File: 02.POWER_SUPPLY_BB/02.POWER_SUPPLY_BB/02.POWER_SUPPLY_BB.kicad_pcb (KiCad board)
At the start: 2 copper layers, 36.1 x 55.1 mm, 17 parts, among them J1 Conn_01x02_Pin, J2 Conn_01x02_Pin, J3 Conn_01x03_Pin, J4 Conn_01x03_Pin, J5 Screw_Terminal_01x02, J6 Barrel_Jack_Switch, J7 Screw_Terminal_01x02, U1 LM7806_TO220, U2 LM317_TO-220

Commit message: UI
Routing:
- net /3.3v: track 0.00 -> 138.7 mm, vias 0 -> 4
- net GND: track 0.00 -> 120.7 mm
- net /PWR_output: track 0.00 -> 100.6 mm
- net /12V: track 0.00 -> 64.3 mm, vias 0 -> 3
- net /5V: track 0.00 -> 61.3 mm
- net Net-(U2-ADJ): track 0.00 -> 42.4 mm
- net /PWR_input: track 0.00 -> 41.4 mm
- net Net-(D1-A): track 0.00 -> 10.6 mm
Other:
- board text added: "Gobal Krishnan V Practice 0.0.2"

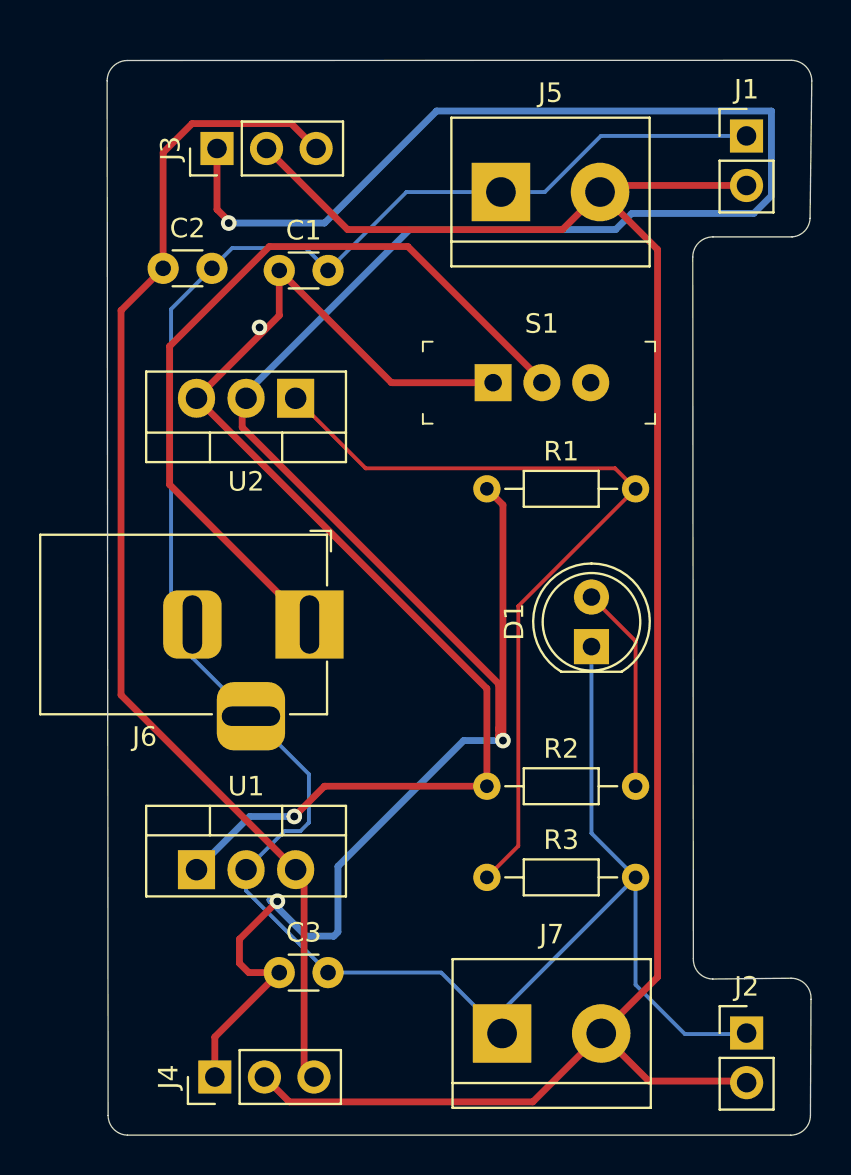
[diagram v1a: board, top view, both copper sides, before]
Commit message: POWER SUPPLY BB - PCB - CHANGE AUTO ROUTING
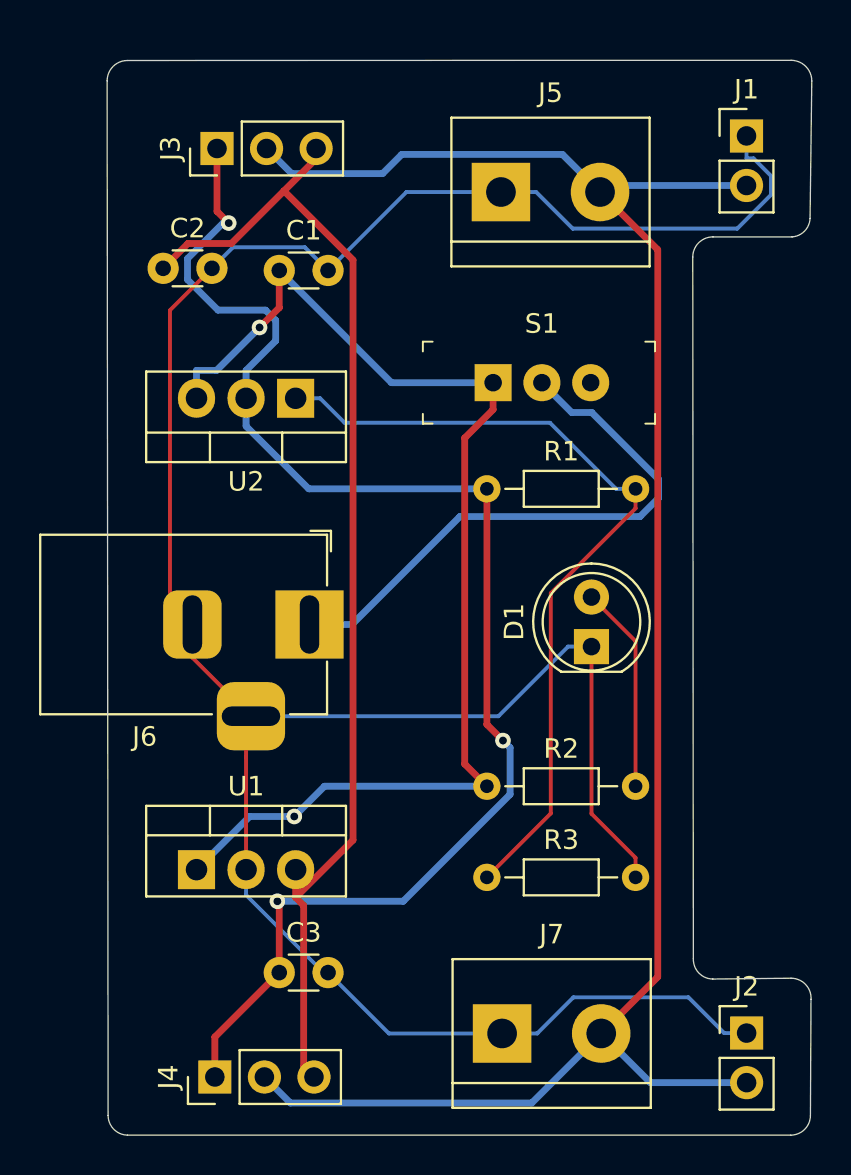
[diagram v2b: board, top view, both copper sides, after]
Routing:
- net /3.3v: track 138.7 -> 73.9 mm
- net GND: track 120.7 -> 133.1 mm
- net /PWR_input: track 41.4 -> 29.6 mm
- net /12V: track 64.3 -> 60.7 mm
- net /PWR_output: track 100.6 -> 99.8 mm
- net /5V: track 61.3 -> 60.6 mm

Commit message: 02.POWER_SUPPLY_BB - PCB - SILKSCREEN
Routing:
- added copper zone on B.Cu, net GND
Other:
- board text added: "3.3v"
- board text added: "5V"
